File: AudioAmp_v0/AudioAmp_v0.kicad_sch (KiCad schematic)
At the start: 78 parts, among them J1 AudioJack3, J2 Conn_01x02_Pin, J3 Connector_RCJ-042, J4 Connector_RCJ-042, J5 AudioJack3, J6 Conn_01x02_Pin, J7 Conn_01x02_Pin, Q1 NMOS_ MTB7D0N6RJ3, Q2 PMOS_MTP4835I3, Q3 NMOS_BSS138, Q4 PMOS_BSS84, Q5 PMOS_BSS84, Q6 PMOS_MTP4835I3, Q7 NMOS_BSS138, Q8 NMOS_ MTB7D0N6RJ3, SW1 SW_DPDT_x2, SW2 SW_DPDT_x2, U1 MAU108, U2 NJM5532, U3 NJM5532

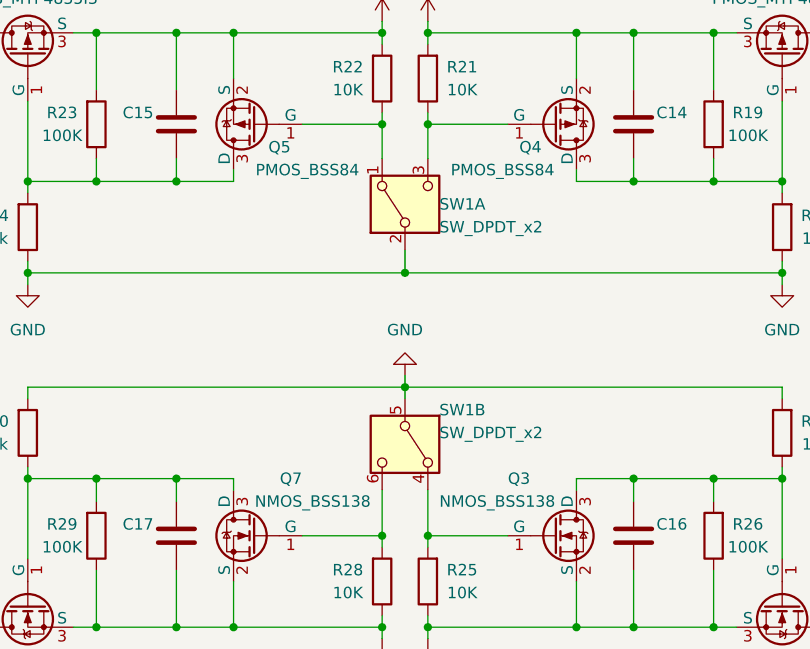
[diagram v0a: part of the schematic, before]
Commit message: スイッチの方向修正
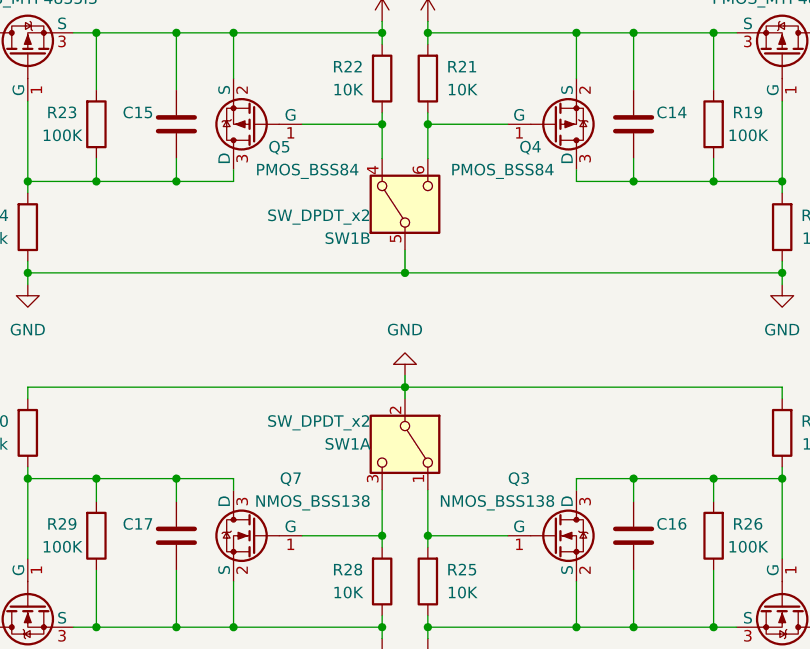
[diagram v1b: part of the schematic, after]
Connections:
- net at Q3.1 (G), R25.2: now also SW1.1 (A); no longer SW1.4 (A)
- net at Q7.1 (G), R28.2: now also SW1.3 (C); no longer SW1.6 (C)
- net at Q5.1 (G), R22.1: now also SW1.4 (A); no longer SW1.1 (A)
- net at Q4.1 (G), R21.1: now also SW1.6 (C); no longer SW1.3 (C)
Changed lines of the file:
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@@
-    )
-  )
-  (symbol (lib_id "Switch:SW_DPDT_x2") (at 72.39 160.02 270) (unit 2)
-    (in_bom yes) (on_board yes) (dnp no)
-    (property "Reference" "SW1" (at 76.2 156.21 90)
-      (effects (font (size 1.27 1.27)) (justify left))
-    )
-    (property "Value" "SW_DPDT_x2" (at 76.2 158.75 90)
-      (effects (font (size 1.27 1.27)) (justify left))
-    )
-    (property "Footprint" "Button_Switch_THT:SW_CK_JS202011CQN_DPDT_Straight" (at 72.39 160.02 0)
-      (effects (font (size 1.27 1.27)) hide)
-    )
-    (property "Datasheet" "~" (at 72.39 160.02 0)
-      (effects (font (size 1.27 1.27)) hide)
-    )
-    (pin "1")
-    (pin "3")
-    (pin "5")
-    (pin "6")
-    (pin "2")
-    (pin "4")
-    (instances
-      (project "AudioAmp_v0"
-        (path "/4f57bce5-a0af-4dee-a148-d94d96167cd8"
-          (reference "SW1") (unit 2)
-        )
-      )
     )
   )
@@
     )
   )
-  (symbol (lib_id "Switch:SW_DPDT_x2") (at 72.39 133.35 90) (unit 1)
-    (in_bom yes) (on_board yes) (dnp no)
-    (property "Reference" "SW1" (at 76.2 133.35 90)
-      (effects (font (size 1.27 1.27)) (justify right))
-    )
-    (property "Value" "SW_DPDT_x2" (at 76.2 135.89 90)
-      (effects (font (size 1.27 1.27)) (justify right))
-    )
-    (property "Footprint" "Button_Switch_THT:SW_CK_JS202011CQN_DPDT_Straight" (at 72.39 133.35 0)
-      (effects (font (size 1.27 1.27)) hide)
-    )
-    (property "Datasheet" "~" (at 72.39 133.35 0)
-      (effects (font (size 1.27 1.27)) hide)
-    )
-    (pin "1")
-    (pin "3")
-    (pin "5")
-    (pin "6")
-    (pin "2")
-    (pin "4")
-    (instances
-      (project "AudioAmp_v0"
-        (path "/4f57bce5-a0af-4dee-a148-d94d96167cd8"
-          (reference "SW1") (unit 1)
-        )
-      )
-    )
-  )
   (symbol (lib_id "power:GND") (at 114.3 142.24 0) (unit 1)
     (in_bom yes) (on_board yes) (dnp no) (fields_autoplaced)
@@
     )
   )
+  (symbol (lib_id "Switch:SW_DPDT_x2") (at 72.39 133.35 90) (unit 2)
+    (in_bom yes) (on_board yes) (dnp no)
+    (property "Reference" "SW1" (at 68.58 137.16 90)
+      (effects (font (size 1.27 1.27)) (justify left))
+    )
+    (property "Value" "SW_DPDT_x2" (at 68.58 134.62 90)
+      (effects (font (size 1.27 1.27)) (justify left))
+    )
+    (property "Footprint" "Button_Switch_THT:SW_CK_JS202011CQN_DPDT_Straight" (at 72.39 133.35 0)
+      (effects (font (size 1.27 1.27)) hide)
+    )
+    (property "Datasheet" "~" (at 72.39 133.35 0)
+      (effects (font (size 1.27 1.27)) hide)
+    )
+    (pin "1")
+    (pin "3")
+    (pin "5")
+    (pin "6")
+    (pin "2")
+    (pin "4")
+    (instances
+      (project "AudioAmp_v0"
+        (path "/4f57bce5-a0af-4dee-a148-d94d96167cd8"
+          (reference "SW1") (unit 2)
+        )
+      )
+    )
+  )
   (symbol (lib_id "Device:R") (at 69.85 119.38 0) (mirror x) (unit 1)
     (in_bom yes) (on_board yes) (dnp no)
@@
         )
       )
+    )
+  )
+  (symbol (lib_id "Switch:SW_DPDT_x2") (at 72.39 160.02 270) (unit 1)
+    (in_bom yes) (on_board yes) (dnp no)
+    (property "Reference" "SW1" (at 68.58 160.02 90)
+      (effects (font (size 1.27 1.27)) (justify right))
+    )
+    (property "Value" "SW_DPDT_x2" (at 68.58 157.48 90)
+      (effects (font (size 1.27 1.27)) (justify right))
+    )
+    (property "Footprint" "Button_Switch_THT:SW_CK_JS202011CQN_DPDT_Straight" (at 72.39 160.02 0)
+      (effects (font (size 1.27 1.27)) hide)
+    )
+    (property "Datasheet" "~" (at 72.39 160.02 0)
+      (effects (font (size 1.27 1.27)) hide)
+    )
+    (pin "1")
+    (pin "3")
+    (pin "5")
+    (pin "6")
+    (pin "2")
+    (pin "4")
+    (instances
+      (project "AudioAmp_v0"
+        (path "/4f57bce5-a0af-4dee-a148-d94d96167cd8"
+          (reference "SW1") (unit 1)
+        )
+      )
